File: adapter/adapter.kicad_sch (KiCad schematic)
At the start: 20 parts, among them J1 Conn_01x06_Female, J2 Conn_01x01_Female, J5 Conn_01x01_Female, SW1 RotaryEncoder_Switch

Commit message: tailor
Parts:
- removed J2, J5: Conn_01x01_Female, Library:1_PinHeader, symbol Connector:Conn_01x01_Female
- removed JP1: SolderJumper_3_Open, Library:SolderJumper-3_P1.3mm_Open_RoundedPad1.0x1.5mm, symbol Jumper:SolderJumper_3_Open
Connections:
- net Col: now also J1.6 (Pin_6)
- net DIN: no longer J1.5 (Pin_5)
- net button: now also J1.5 (Pin_5); no longer J1.2 (Pin_2)
- net r1: now also J1.2 (Pin_2); no longer J1.4 (Pin_4)
- net at SW1.S1: now also Dcol1.2 (A)
- net +5V renamed Vcc
- net Vcc: no longer J1.1 (Pin_1)
- net GND renamed Gnd
- net Gnd: now also J1.1 (Pin_1); no longer J1.6 (Pin_6)
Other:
- note removed: "To trackball connector"
- moved on the sheet: Dcol1

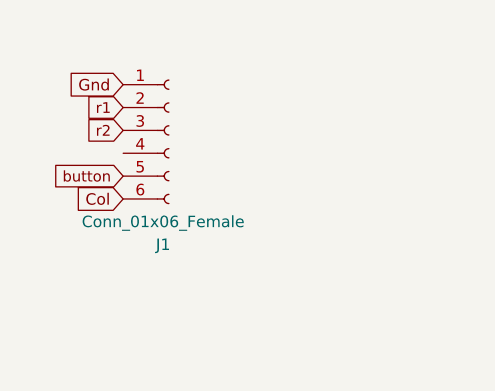
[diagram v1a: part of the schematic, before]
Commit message: rearrange to avoid cable twist
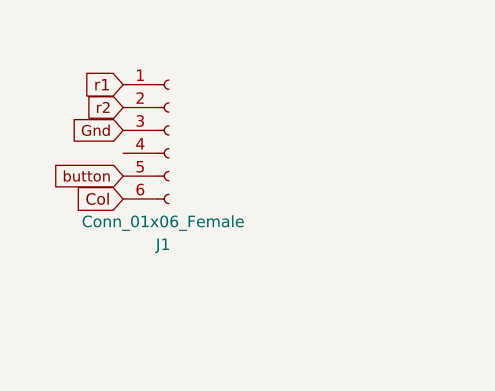
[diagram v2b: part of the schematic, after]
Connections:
- net Gnd: now also J1.3 (Pin_3); no longer J1.1 (Pin_1)
- net r1: now also J1.1 (Pin_1); no longer J1.2 (Pin_2)
- net r2: now also J1.2 (Pin_2); no longer J1.3 (Pin_3)
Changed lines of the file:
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@@
     (effects (font (size 1.27 1.27)) (justify right bottom))
   )
-  (global_label "r1" (shape input) (at 35.56 36.83 180) (fields_autoplaced)
+  (global_label "r2" (shape input) (at 35.56 36.83 180) (fields_autoplaced)
     (effects (font (size 1.1938 1.1938)) (justify right))
-    (property "Intersheetrefs" "${INTERSHEET_REFS}" (at 31.2368 36.7554 0)
+    (property "Intersheetrefs" "${INTERSHEET_REFS}" (at 30.7891 36.83 0)
       (effects (font (size 1.1938 1.1938)) (justify right) hide)
     )
@@
     )
   )
-  (global_label "r2" (shape input) (at 35.56 39.37 180) (fields_autoplaced)
+  (global_label "Gnd" (shape input) (at 35.56 39.37 180) (fields_autoplaced)
     (effects (font (size 1.1938 1.1938)) (justify right))
-    (property "Intersheetrefs" "${INTERSHEET_REFS}" (at 31.2368 39.2954 0)
+    (property "Intersheetrefs" "${INTERSHEET_REFS}" (at 29.3111 39.37 0)
       (effects (font (size 1.1938 1.1938)) (justify right) hide)
     )
@@
     )
   )
-  (global_label "Gnd" (shape input) (at 35.56 34.29 180) (fields_autoplaced)
+  (global_label "r1" (shape input) (at 35.56 34.29 180) (fields_autoplaced)
     (effects (font (size 1.27 1.27)) (justify right))
-    (property "Intersheetrefs" "${INTERSHEET_REFS}" (at 29.3883 34.2106 0)
+    (property "Intersheetrefs" "${INTERSHEET_REFS}" (at 30.484 34.29 0)
       (effects (font (size 1.27 1.27)) (justify right) hide)
     )

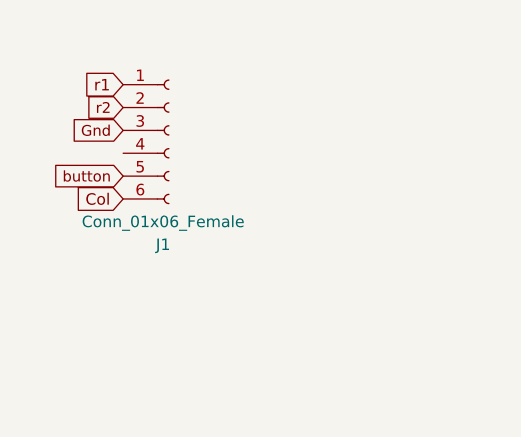
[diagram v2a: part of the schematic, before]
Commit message: route without break
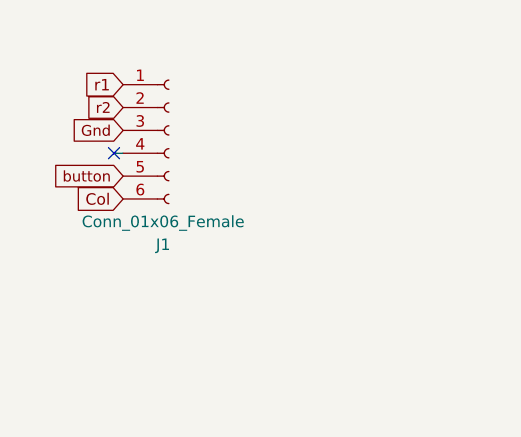
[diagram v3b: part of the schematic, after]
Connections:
- no-connect marks 0 -> 1
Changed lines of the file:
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@@
   (junction (at 118.11 102.87) (diameter 0) (color 0 0 0 0)
   )
+  (no_connect (at 34.544 41.91))
   (wire (pts (xy 162.56 95.25) (xy 165.1 95.25))
     (stroke (width 0) (type default))
   )
+  (wire (pts (xy 34.544 41.91) (xy 35.56 41.91))
+    (stroke (width 0) (type default))
+  )
